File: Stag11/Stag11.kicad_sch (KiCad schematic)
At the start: 2 parts

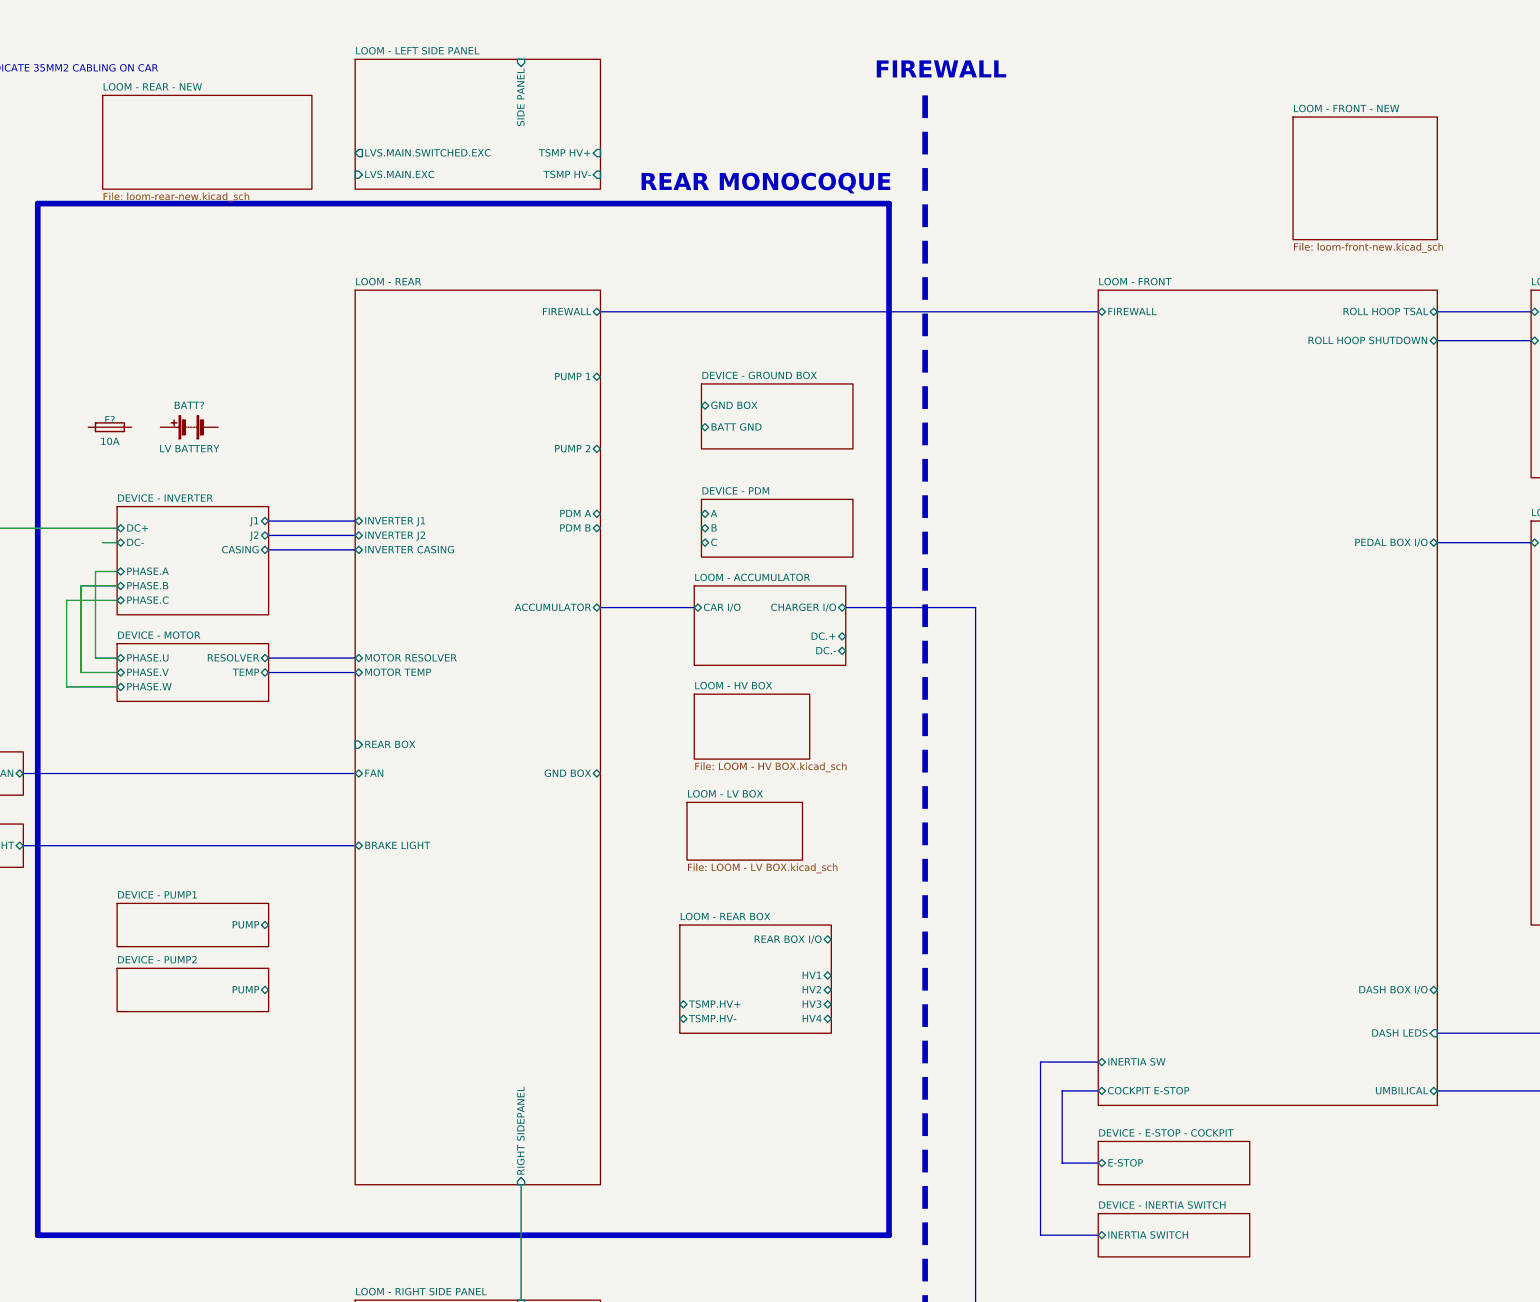
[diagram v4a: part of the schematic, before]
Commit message: Changed top level loom
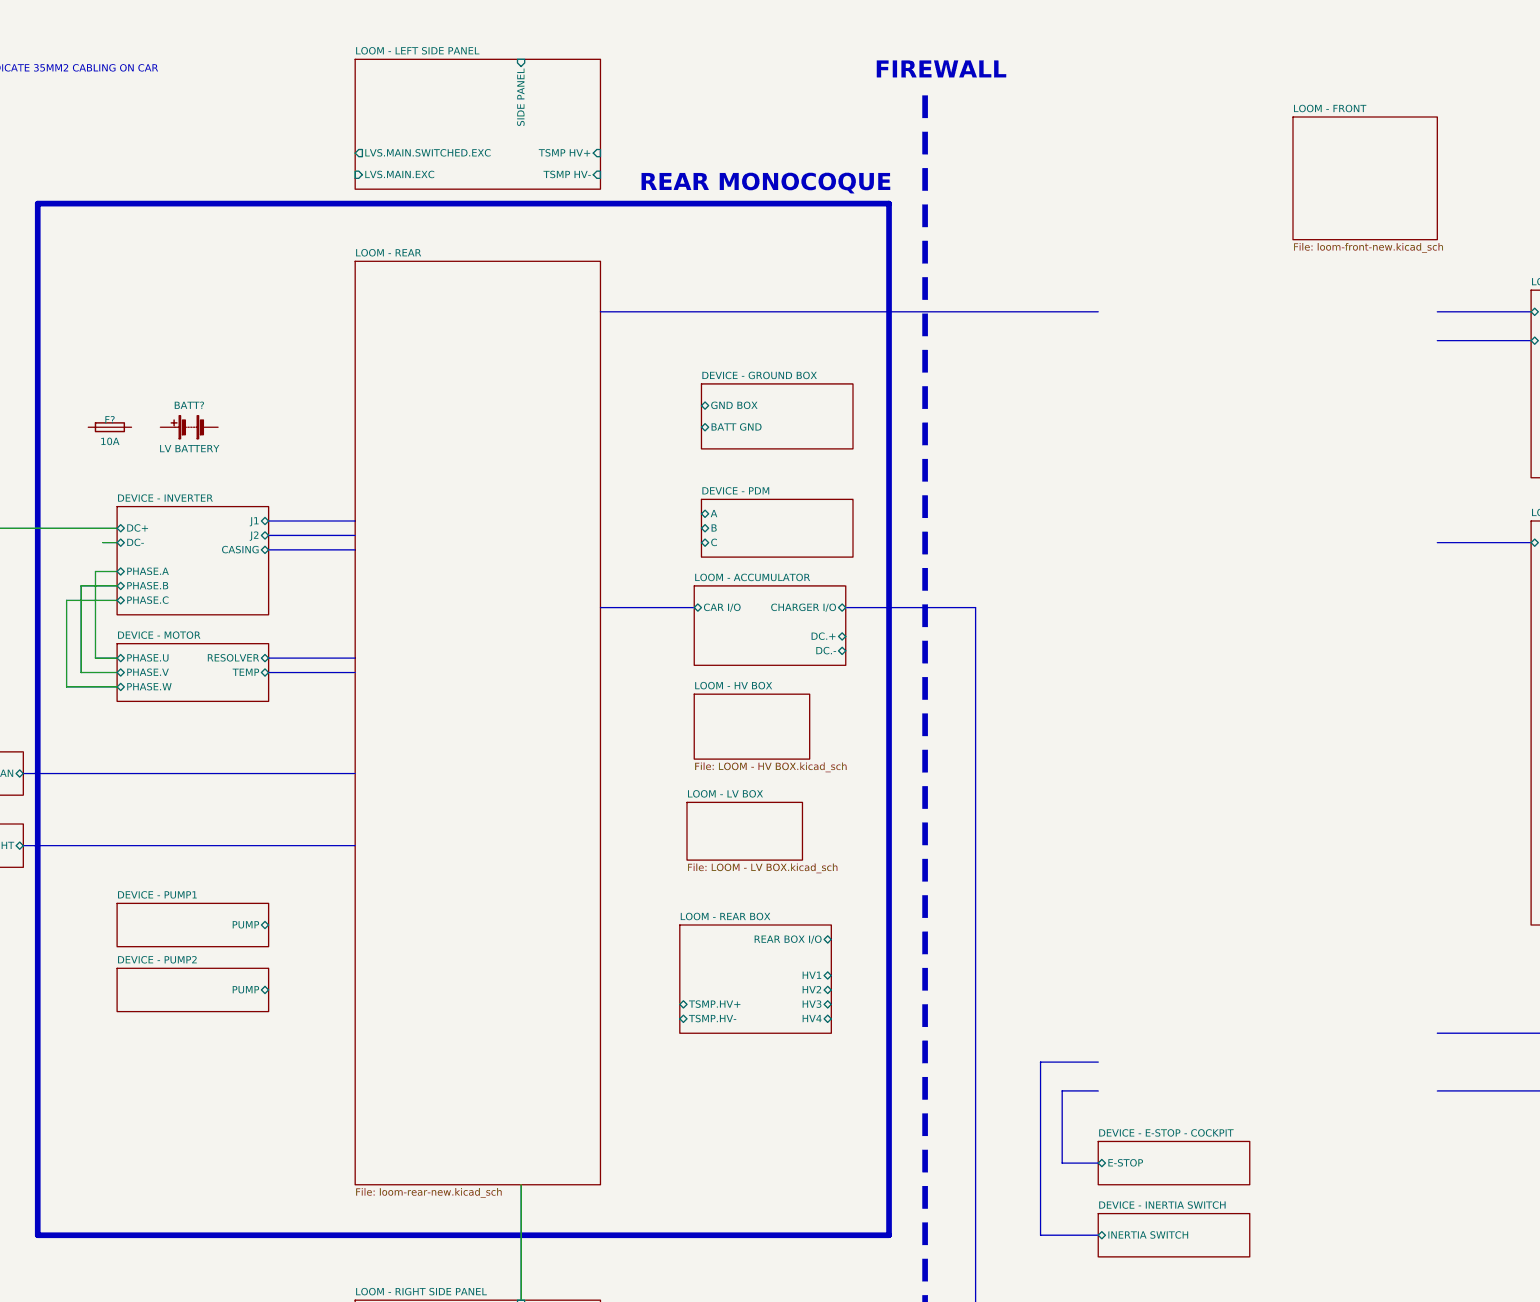
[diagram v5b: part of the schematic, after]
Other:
- removed sheet LOOM - FRONT - NEW
- removed sheet LOOM - REAR - NEW
- sheet LOOM - FRONT: file loom-front.kicad_sch -> loom-front-new.kicad_sch
- sheet LOOM - FRONT ports: added none; removed COCKPIT E-STOP, DASH BOX I/O, DASH LEDS, FIREWALL, INERTIA SW, PEDAL BOX I/O, ROLL HOOP SHUTDOWN, ROLL HOOP TSAL, UMBILICAL
- sheet LOOM - REAR: file loom-rear.kicad_sch -> loom-rear-new.kicad_sch
- sheet LOOM - REAR ports: added none; removed ACCUMULATOR, BRAKE LIGHT, FAN, FIREWALL, GND BOX, INVERTER CASING, INVERTER J1, INVERTER J2, MOTOR RESOLVER, MOTOR TEMP, PDM A, PDM B, PUMP 1, PUMP 2, REAR BOX, RIGHT SIDEPANEL

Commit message: Reordered shutdown loop and spliced power in LV box
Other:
- removed sheet LOOM - REAR BOX
- sheet LOOM - FRONT ports: added COCKPIT E-STOP, DASHBOARD, FIREWALL, INERTIA SW, PEDAL BOX I/O, ROLL HOOP SHUTDOWN, ROLL HOOP TSAL, SAGL; removed none
- sheet LOOM - HV BOX ports: added BSPD CT, HV Connector, HV1, HV2, HV3, HV4, LV - HV Connector, TSMP.HV+, TSMP.HV-; removed none
- sheet LOOM - LV BOX ports: added LV - HV Connector, Main LV connector; removed none
- sheet LOOM - REAR ports: added ACCUMULATOR, BRAKE LIGHT, FAN, FIREWALL, GND BOX, HV Connector, HV IN, HV OUT, INVERTER CASING, INVERTER J1, INVERTER J2, MOTOR RESOLVER, MOTOR TEMP, Main LV connector, PDM A, PDM B, PUMP 1, PUMP 2, SIDEPANEL - RHS, UMBILICAL; removed none
- note added: "HVD"
